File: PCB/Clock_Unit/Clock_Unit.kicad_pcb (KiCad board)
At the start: 2 copper layers, 50 x 50 mm, 106 parts, among them J1 Conn_01x04, J2 Conn_01x04, J3 Conn_01x04, J4 Conn_01x04

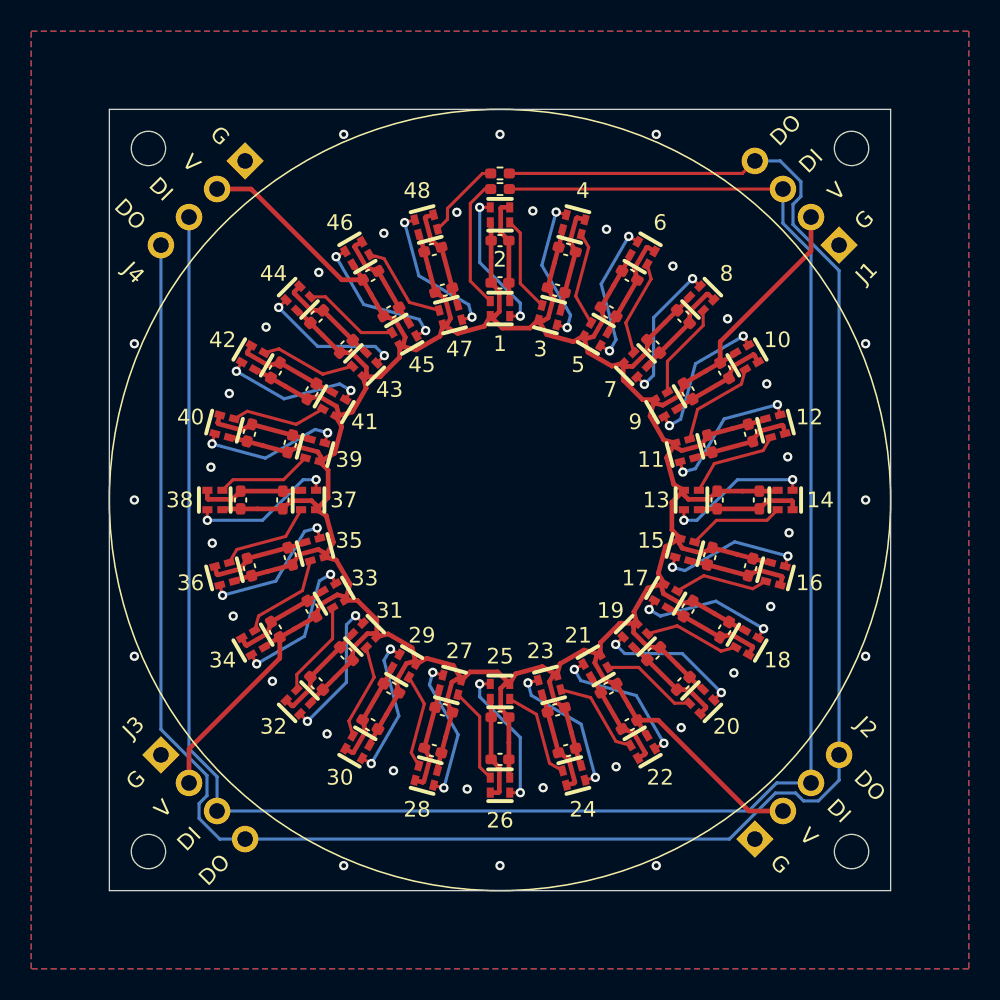
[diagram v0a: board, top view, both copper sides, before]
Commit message: Increase VDD trace width
Chanced from 0.3mm to 1mm to support max power draw of all LEDs
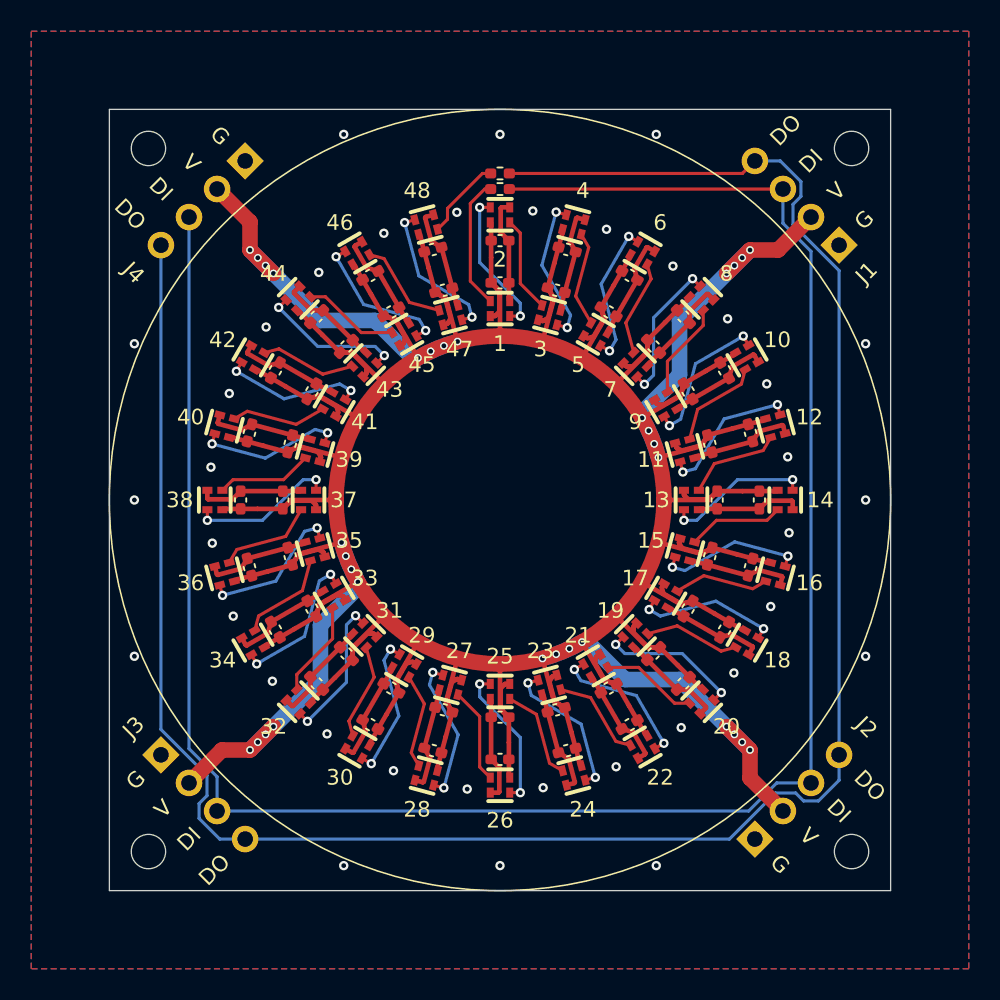
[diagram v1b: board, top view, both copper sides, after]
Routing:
- net /VDD: track 291.3 -> 402.1 mm, vias 0 -> 32

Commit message: Add center hole
m3 opening added
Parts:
- added H5: MountingHole, MountingHole:MountingHole_3.2mm_M3, F.Cu at (130.0, 100.0)
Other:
- board text added: "LED_CCC_Mini V1.0 Andy D 2x R=220 48x C=104"
- board text removed: "LED_CCC_Mini V1.0 By Andy D All R=220 All C=104"

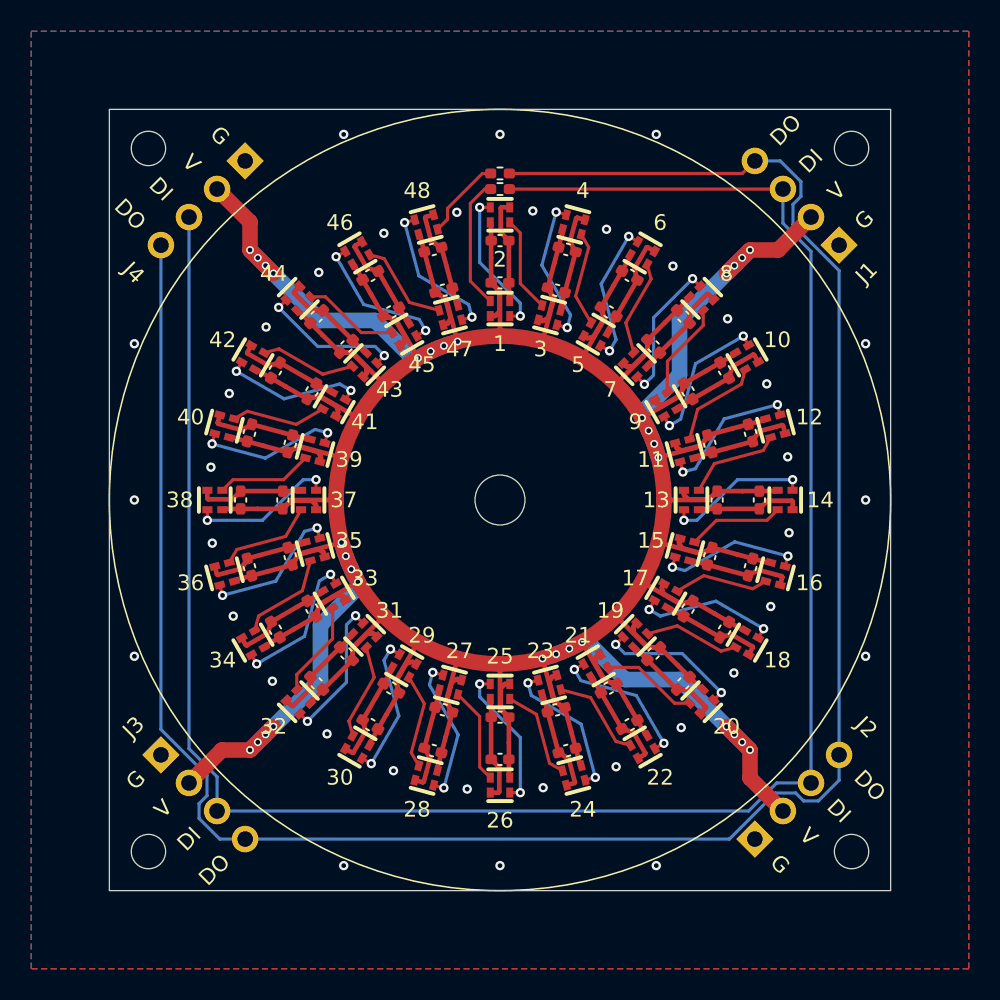
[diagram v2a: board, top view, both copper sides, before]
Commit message: Schematic + PCB Updates
Corrected LED symbol and improved silkscreen
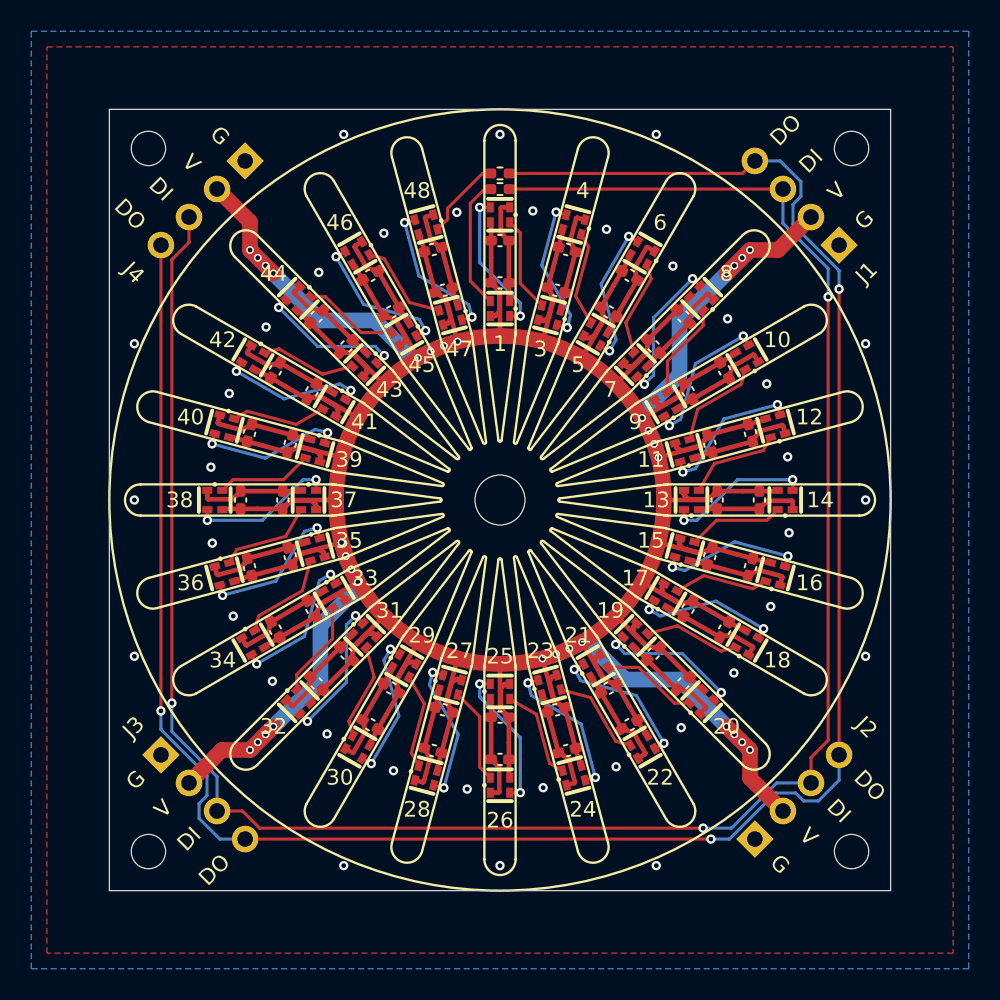
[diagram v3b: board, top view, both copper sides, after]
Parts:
- H1, H2, H3, H4: value MountingHole -> Corner_m2_Hole
- H5: value MountingHole -> Center_m3_Hole
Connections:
- C1 pad 1: /VDD -> VDD
- C1 pad 2: /GND -> GND
- C10 pad 1: /VDD -> VDD
- C10 pad 2: /GND -> GND
- C11 pad 1: /VDD -> VDD
- C11 pad 2: /GND -> GND
- C12 pad 1: /VDD -> VDD
- C12 pad 2: /GND -> GND
- C13 pad 1: /VDD -> VDD
- C13 pad 2: /GND -> GND
- C14 pad 1: /VDD -> VDD
- C14 pad 2: /GND -> GND
- C15 pad 1: /VDD -> VDD
- C15 pad 2: /GND -> GND
- C16 pad 1: /VDD -> VDD
- C16 pad 2: /GND -> GND
- C17 pad 1: /VDD -> VDD
- C17 pad 2: /GND -> GND
- C18 pad 1: /VDD -> VDD
- C18 pad 2: /GND -> GND
- C19 pad 1: /VDD -> VDD
- C19 pad 2: /GND -> GND
- C2 pad 1: /VDD -> VDD
- C2 pad 2: /GND -> GND
- C20 pad 1: /VDD -> VDD
- C20 pad 2: /GND -> GND
- C21 pad 1: /VDD -> VDD
- C21 pad 2: /GND -> GND
- C22 pad 1: /VDD -> VDD
- C22 pad 2: /GND -> GND
- C23 pad 1: /VDD -> VDD
- C23 pad 2: /GND -> GND
- C24 pad 1: /VDD -> VDD
- C24 pad 2: /GND -> GND
- C25 pad 1: /VDD -> VDD
- C25 pad 2: /GND -> GND
- C26 pad 1: /VDD -> VDD
- C26 pad 2: /GND -> GND
- C27 pad 1: /VDD -> VDD
- C27 pad 2: /GND -> GND
- C28 pad 1: /VDD -> VDD
- C28 pad 2: /GND -> GND
- C29 pad 1: /VDD -> VDD
- C29 pad 2: /GND -> GND
- C3 pad 1: /VDD -> VDD
- C3 pad 2: /GND -> GND
- C30 pad 1: /VDD -> VDD
- C30 pad 2: /GND -> GND
- C31 pad 1: /VDD -> VDD
- C31 pad 2: /GND -> GND
- C32 pad 1: /VDD -> VDD
- C32 pad 2: /GND -> GND
- C33 pad 1: /VDD -> VDD
- C33 pad 2: /GND -> GND
- C34 pad 1: /VDD -> VDD
- C34 pad 2: /GND -> GND
- C35 pad 1: /VDD -> VDD
- C35 pad 2: /GND -> GND
- C36 pad 1: /VDD -> VDD
- C36 pad 2: /GND -> GND
- C37 pad 1: /VDD -> VDD
- C37 pad 2: /GND -> GND
- C38 pad 1: /VDD -> VDD
- C38 pad 2: /GND -> GND
- C39 pad 1: /VDD -> VDD
- C39 pad 2: /GND -> GND
- C4 pad 1: /VDD -> VDD
- C4 pad 2: /GND -> GND
- C40 pad 1: /VDD -> VDD
- C40 pad 2: /GND -> GND
- C41 pad 1: /VDD -> VDD
- C41 pad 2: /GND -> GND
- C42 pad 1: /VDD -> VDD
- C42 pad 2: /GND -> GND
- C43 pad 1: /VDD -> VDD
- C43 pad 2: /GND -> GND
- C44 pad 1: /VDD -> VDD
- C44 pad 2: /GND -> GND
- C45 pad 1: /VDD -> VDD
- C45 pad 2: /GND -> GND
- C46 pad 1: /VDD -> VDD
- C46 pad 2: /GND -> GND
- C47 pad 1: /VDD -> VDD
- C47 pad 2: /GND -> GND
- C48 pad 1: /VDD -> VDD
- C48 pad 2: /GND -> GND
- C5 pad 1: /VDD -> VDD
- C5 pad 2: /GND -> GND
- C6 pad 1: /VDD -> VDD
- C6 pad 2: /GND -> GND
- C7 pad 1: /VDD -> VDD
- C7 pad 2: /GND -> GND
- C8 pad 1: /VDD -> VDD
- C8 pad 2: /GND -> GND
- C9 pad 1: /VDD -> VDD
- C9 pad 2: /GND -> GND
- J1 pad 1: /GND -> GND
- J1 pad 2: /VDD -> VDD
- J2 pad 1: /GND -> GND
- J2 pad 2: /VDD -> VDD
- J3 pad 1: /GND -> GND
- J3 pad 2: /VDD -> VDD
- J4 pad 1: /GND -> GND
- J4 pad 2: /VDD -> VDD
- LED1 pad 1: Net-(LED1-DO) -> GND
- LED1 pad 2: /VDD -> /LEDSpoke1/DI
- LED1 pad 3: /GND -> VDD
- LED1 pad 4: /LEDSpoke1/DI -> Net-(LED1-DO)
- LED10 pad 1: /LEDSpoke5/DO -> GND
- LED10 pad 2: /VDD -> Net-(LED10-VDD)
- LED10 pad 3: /GND -> VDD
- LED10 pad 4: Net-(LED10-DI) -> /LEDSpoke5/DO
- LED11 pad 1: Net-(LED11-DO) -> GND
- LED11 pad 2: /VDD -> /LEDSpoke5/DO
- LED11 pad 3: /GND -> VDD
- LED11 pad 4: /LEDSpoke5/DO -> Net-(LED11-DI)
- LED12 pad 1: /LEDSpoke6/DO -> GND
- LED12 pad 2: /VDD -> Net-(LED11-DI)
- LED12 pad 3: /GND -> VDD
- LED12 pad 4: Net-(LED11-DO) -> /LEDSpoke6/DO
- LED13 pad 1: Net-(LED13-DO) -> GND
- LED13 pad 2: /VDD -> /LEDSpoke6/DO
- LED13 pad 3: /GND -> VDD
- LED13 pad 4: /LEDSpoke6/DO -> Net-(LED13-DI)
- LED14 pad 1: /LEDSpoke7/DO -> GND
- LED14 pad 2: /VDD -> Net-(LED13-DI)
- LED14 pad 3: /GND -> VDD
- LED14 pad 4: Net-(LED13-DO) -> /LEDSpoke7/DO
- LED15 pad 1: Net-(LED15-DO) -> GND
- LED15 pad 2: /VDD -> /LEDSpoke7/DO
- LED15 pad 3: /GND -> VDD
- LED15 pad 4: /LEDSpoke7/DO -> Net-(LED15-DI)
- LED16 pad 1: /LEDSpoke8/DO -> GND
- LED16 pad 2: /VDD -> Net-(LED15-DI)
- LED16 pad 3: /GND -> VDD
- LED16 pad 4: Net-(LED15-DO) -> /LEDSpoke8/DO
- LED17 pad 1: Net-(LED17-DO) -> GND
- LED17 pad 2: /VDD -> /LEDSpoke8/DO
- LED17 pad 3: /GND -> VDD
- LED17 pad 4: /LEDSpoke8/DO -> Net-(LED17-DI)
- LED18 pad 1: /LEDSpoke10/DI -> GND
- LED18 pad 2: /VDD -> Net-(LED17-DI)
- LED18 pad 3: /GND -> VDD
- LED18 pad 4: Net-(LED17-DO) -> /LEDSpoke10/DI
- LED19 pad 1: Net-(LED19-DO) -> GND
- LED19 pad 2: /VDD -> /LEDSpoke10/DI
- LED19 pad 3: /GND -> VDD
- LED19 pad 4: /LEDSpoke10/DI -> Net-(LED19-DI)
- LED2 pad 1: /LEDSpoke1/DO -> GND
- LED2 pad 2: /VDD -> Net-(LED1-DO)
- LED2 pad 3: /GND -> VDD
- LED2 pad 4: Net-(LED1-DO) -> /LEDSpoke1/DO
- LED20 pad 1: /LEDSpoke10/DO -> GND
- LED20 pad 2: /VDD -> Net-(LED19-DI)
- LED20 pad 3: /GND -> VDD
- LED20 pad 4: Net-(LED19-DO) -> /LEDSpoke10/DO
- LED21 pad 1: Net-(LED21-DO) -> GND
- LED21 pad 2: /VDD -> /LEDSpoke10/DO
- LED21 pad 3: /GND -> VDD
- LED21 pad 4: /LEDSpoke10/DO -> Net-(LED21-DI)
- LED22 pad 1: /LEDSpoke11/DO -> GND
- LED22 pad 2: /VDD -> Net-(LED21-DI)
- LED22 pad 3: /GND -> VDD
- LED22 pad 4: Net-(LED21-DO) -> /LEDSpoke11/DO
- LED23 pad 1: Net-(LED23-DO) -> GND
- LED23 pad 2: /VDD -> /LEDSpoke11/DO
- LED23 pad 3: /GND -> VDD
- LED23 pad 4: /LEDSpoke11/DO -> Net-(LED23-DI)
- LED24 pad 1: /LEDSpoke12/DO -> GND
- LED24 pad 2: /VDD -> Net-(LED23-DI)
- LED24 pad 3: /GND -> VDD
- LED24 pad 4: Net-(LED23-DO) -> /LEDSpoke12/DO
- LED25 pad 1: Net-(LED25-DO) -> GND
- LED25 pad 2: /VDD -> /LEDSpoke12/DO
- LED25 pad 3: /GND -> VDD
- LED25 pad 4: /LEDSpoke12/DO -> Net-(LED25-DI)
- LED26 pad 1: /LEDSpoke13/DO -> GND
- LED26 pad 2: /VDD -> Net-(LED25-DI)
- LED26 pad 3: /GND -> VDD
- LED26 pad 4: Net-(LED25-DO) -> /LEDSpoke13/DO
- LED27 pad 1: Net-(LED27-DO) -> GND
- LED27 pad 2: /VDD -> /LEDSpoke13/DO
- LED27 pad 3: /GND -> VDD
- LED27 pad 4: /LEDSpoke13/DO -> Net-(LED27-DI)
- LED28 pad 1: /LEDSpoke14/DO -> GND
- LED28 pad 2: /VDD -> Net-(LED27-DI)
- LED28 pad 3: /GND -> VDD
- LED28 pad 4: Net-(LED27-DO) -> /LEDSpoke14/DO
- LED29 pad 1: Net-(LED29-DO) -> GND
- LED29 pad 2: /VDD -> /LEDSpoke14/DO
- LED29 pad 3: /GND -> VDD
- LED29 pad 4: /LEDSpoke14/DO -> Net-(LED29-DI)
- LED3 pad 1: Net-(LED3-DO) -> GND
- LED3 pad 2: /VDD -> /LEDSpoke1/DO
- LED3 pad 3: /GND -> VDD
- LED3 pad 4: /LEDSpoke1/DO -> Net-(LED3-DI)
- LED30 pad 1: /LEDSpoke15/DO -> GND
- LED30 pad 2: /VDD -> Net-(LED29-DI)
- LED30 pad 3: /GND -> VDD
- LED30 pad 4: Net-(LED29-DO) -> /LEDSpoke15/DO
- LED31 pad 1: Net-(LED31-DO) -> GND
- LED31 pad 2: /VDD -> /LEDSpoke15/DO
- LED31 pad 3: /GND -> VDD
- LED31 pad 4: /LEDSpoke15/DO -> Net-(LED31-DI)
- LED32 pad 1: /LEDSpoke16/DO -> GND
- LED32 pad 2: /VDD -> Net-(LED31-DI)
- LED32 pad 3: /GND -> VDD
- LED32 pad 4: Net-(LED31-DO) -> /LEDSpoke16/DO
- LED33 pad 1: Net-(LED33-DO) -> GND
- LED33 pad 2: /VDD -> /LEDSpoke16/DO
- LED33 pad 3: /GND -> VDD
- LED33 pad 4: /LEDSpoke16/DO -> Net-(LED33-DI)
- LED34 pad 1: /LEDSpoke17/DO -> GND
- LED34 pad 2: /VDD -> Net-(LED33-DI)
- LED34 pad 3: /GND -> VDD
- LED34 pad 4: Net-(LED33-DO) -> /LEDSpoke17/DO
- LED35 pad 1: Net-(LED35-DO) -> GND
- LED35 pad 2: /VDD -> /LEDSpoke17/DO
- LED35 pad 3: /GND -> VDD
- LED35 pad 4: /LEDSpoke17/DO -> Net-(LED35-DI)
- LED36 pad 1: /LEDSpoke18/DO -> GND
- LED36 pad 2: /VDD -> Net-(LED35-DI)
- LED36 pad 3: /GND -> VDD
- LED36 pad 4: Net-(LED35-DO) -> /LEDSpoke18/DO
- LED37 pad 1: Net-(LED37-DO) -> GND
- LED37 pad 2: /VDD -> /LEDSpoke18/DO
- LED37 pad 3: /GND -> VDD
- LED37 pad 4: /LEDSpoke18/DO -> Net-(LED37-DI)
- LED38 pad 1: /LEDSpoke19/DO -> GND
- LED38 pad 2: /VDD -> Net-(LED37-DI)
- LED38 pad 3: /GND -> VDD
- LED38 pad 4: Net-(LED37-DO) -> /LEDSpoke19/DO
- LED39 pad 1: Net-(LED39-DO) -> GND
- LED39 pad 2: /VDD -> /LEDSpoke19/DO
- LED39 pad 3: /GND -> VDD
- LED39 pad 4: /LEDSpoke19/DO -> Net-(LED39-DI)
- LED4 pad 1: /LEDSpoke2/DO -> GND
- LED4 pad 2: /VDD -> Net-(LED3-DI)
- LED4 pad 3: /GND -> VDD
- LED4 pad 4: Net-(LED3-DO) -> /LEDSpoke2/DO
- LED40 pad 1: /LEDSpoke20/DO -> GND
- LED40 pad 2: /VDD -> Net-(LED39-DI)
- LED40 pad 3: /GND -> VDD
- LED40 pad 4: Net-(LED39-DO) -> /LEDSpoke20/DO
- LED41 pad 1: Net-(LED41-DO) -> GND
- LED41 pad 2: /VDD -> /LEDSpoke20/DO
- LED41 pad 3: /GND -> VDD
- LED41 pad 4: /LEDSpoke20/DO -> Net-(LED41-DI)
- LED42 pad 1: /LEDSpoke21/DO -> GND
- LED42 pad 2: /VDD -> Net-(LED41-DI)
- LED42 pad 3: /GND -> VDD
- LED42 pad 4: Net-(LED41-DO) -> /LEDSpoke21/DO
- LED43 pad 1: Net-(LED43-DO) -> GND
- LED43 pad 2: /VDD -> /LEDSpoke21/DO
- LED43 pad 3: /GND -> VDD
- LED43 pad 4: /LEDSpoke21/DO -> Net-(LED43-DI)
- LED44 pad 1: /LEDSpoke22/DO -> GND
- LED44 pad 2: /VDD -> Net-(LED43-DI)
- LED44 pad 3: /GND -> VDD
- LED44 pad 4: Net-(LED43-DO) -> /LEDSpoke22/DO
- LED45 pad 1: Net-(LED45-DO) -> GND
- LED45 pad 2: /VDD -> /LEDSpoke22/DO
- LED45 pad 3: /GND -> VDD
- LED45 pad 4: /LEDSpoke22/DO -> Net-(LED45-DI)
- LED46 pad 1: /LEDSpoke23/DO -> GND
- LED46 pad 2: /VDD -> Net-(LED45-DI)
- LED46 pad 3: /GND -> VDD
- LED46 pad 4: Net-(LED45-DO) -> /LEDSpoke23/DO
- LED47 pad 1: Net-(LED47-DO) -> GND
- LED47 pad 2: /VDD -> /LEDSpoke23/DO
- LED47 pad 3: /GND -> VDD
- LED47 pad 4: /LEDSpoke23/DO -> Net-(LED47-DI)
- LED48 pad 1: /LEDSpoke24/DO -> GND
- LED48 pad 2: /VDD -> Net-(LED47-DI)
- LED48 pad 3: /GND -> VDD
- LED48 pad 4: Net-(LED47-DO) -> /LEDSpoke24/DO
- LED5 pad 1: Net-(LED5-DO) -> GND
- LED5 pad 2: /VDD -> /LEDSpoke2/DO
- LED5 pad 3: /GND -> VDD
- LED5 pad 4: /LEDSpoke2/DO -> Net-(LED5-DI)
- LED6 pad 1: /LEDSpoke3/DO -> GND
- LED6 pad 2: /VDD -> Net-(LED5-DI)
- LED6 pad 3: /GND -> VDD
- LED6 pad 4: Net-(LED5-DO) -> /LEDSpoke3/DO
- LED7 pad 1: Net-(LED7-DO) -> GND
- LED7 pad 2: /VDD -> /LEDSpoke3/DO
- LED7 pad 3: /GND -> VDD
- LED7 pad 4: /LEDSpoke3/DO -> Net-(LED7-DI)
- LED8 pad 1: /LEDSpoke4/DO -> GND
- LED8 pad 2: /VDD -> Net-(LED7-DI)
- LED8 pad 3: /GND -> VDD
- LED8 pad 4: Net-(LED7-DO) -> /LEDSpoke4/DO
- LED9 pad 1: Net-(LED10-DI) -> GND
- LED9 pad 2: /VDD -> /LEDSpoke4/DO
- LED9 pad 3: /GND -> VDD
- LED9 pad 4: /LEDSpoke4/DO -> Net-(LED10-VDD)
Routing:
- net VDD: track 0.00 -> 402.1 mm, vias 0 -> 32
- net /VDD: track 402.1 -> 0.00 mm, vias 32 -> 0
- net GND: track 0.00 -> 161.1 mm, vias 0 -> 36
- net /GND: track 161.1 -> 0.00 mm, vias 36 -> 0
- net Net-(LED25-DO): track 9.40 -> 0.00 mm, vias 2 -> 0
- net Net-(LED25-DI): track 0.00 -> 9.40 mm, vias 0 -> 2
- net Net-(LED37-DO): track 9.40 -> 0.00 mm, vias 2 -> 0
- net Net-(LED37-DI): track 0.00 -> 9.40 mm, vias 0 -> 2
- net Net-(LED13-DO): track 9.40 -> 0.00 mm, vias 2 -> 0
- net Net-(LED13-DI): track 0.00 -> 9.40 mm, vias 0 -> 2
- net Net-(LED19-DO): track 9.40 -> 0.00 mm, vias 2 -> 0
- net Net-(LED19-DI): track 0.00 -> 9.40 mm, vias 0 -> 2
- net Net-(LED43-DO): track 9.40 -> 0.00 mm, vias 2 -> 0
- net Net-(LED43-DI): track 0.00 -> 9.40 mm, vias 0 -> 2
- net Net-(LED31-DO): track 9.40 -> 0.00 mm, vias 2 -> 0
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- added copper zone on B.Cu, net GND
- added copper zone on F.Cu, net GND
- removed copper zone on B.Cu, net /GND
- removed copper zone on F.Cu, net /GND
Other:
- board text added: "LED_CCC_Mini v1.0 Aug 2025 2x R=220 48x C=104 48x WS2812B"
- board text removed: "LED_CCC_Mini V1.0 Andy D 2x R=220 48x C=104"
